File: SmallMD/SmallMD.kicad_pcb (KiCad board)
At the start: 2 copper layers, 178 parts, among them J1 Conn_01x02_Male, J2 Conn_01x02_Female, J3 Conn_01x10_Male, J4 Conn_01x02_Female, J5 Conn_01x04_Male, J6 Conn_01x04_Male, J7 Conn_01x10_Male, Q1 SSM6J808R, Q10 S8050, Q11 S8050, Q14 BSS138, Q15 BSS138, Q16 S8050, Q18 μPA2753GR, Q19 μPA2753GR, Q2 BSS138, Q3 SSM6J808R, Q4 SSM3J332R, Q5 SSM3J332R, Q6 S8050, Q7 S8050, Q8 SSM3J332R, Q9 SSM3J332R, SW1 SW_DIP_x05, SW2 SW_SPDT, SW3 SW_SPDT_White, SW4 SW_SPST, U1 AZ1084CD-3.3, U10 IR2302, U11 IR2302, U12 MAX3485, U2 AZ1084CD-5.0, U3 STM32C031K4T6, U4 MAX3485, U5 MAX3485, U6 LT6106, U7 MAX3485, U8 TLP2361, U9 TLP2361, Y1 48MHz

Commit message: 進捗
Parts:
- removed C15, C16: 470uF, Capacitor_SMD:C_Elec_8x10.2
- removed C8: ADJ_ST, Capacitor_SMD:C_0603_1608Metric
- removed D11, D12: Green, LED_SMD:LED_0603_1608Metric_Pad1.05x0.95mm_HandSolder
- removed D9: D_Zener, Diode_SMD:D_SOD-323_HandSoldering
- removed H1, H3: MountingHole_Pad, TestPoint:TestPoint_Pad_1.5x1.5mm
- removed H4, H6, H8: MountingHole, MountingHole:MountingHole_3.2mm_M3
- removed Q10, Q11, Q6, Q7: S8050, Package_TO_SOT_SMD:SOT-23
- removed Q4, Q5, Q8, Q9: SSM3J332R, Package_TO_SOT_SMD:SOT-23W
- removed R20, R21, R24, R25, R26, R27, R28, R29, R30: 10k, Resistor_SMD:R_0402_1005Metric
- removed R22, R32, R33: 1k, Resistor_SMD:R_0402_1005Metric
- removed R23: 100k, Resistor_SMD:R_0402_1005Metric
- added J8: Conn_01x06_Male, Connector_JST:JST_PH_B6B-PH-K_1x06_P2.00mm_Vertical, B.Cu at (87.4, 36.3)
- added JP5: SolderJumper_3_Bridged12, Jumper:SolderJumper-3_P2.0mm_Open_TrianglePad1.0x1.5mm_NumberLabels, F.Cu at (44.0, 47.0)
- added JP6: SolderJumper_3_Bridged12, Jumper:SolderJumper-3_P2.0mm_Open_TrianglePad1.0x1.5mm_NumberLabels, F.Cu at (44.0, 43.4)
- added R39: 40mR, Resistor_SMD:R_2512_6332Metric, F.Cu at (74.0, 11.0)
- added R46: 40mR, Resistor_SMD:R_2512_6332Metric, F.Cu at (74.0, 15.0)
- added R52: 40mR, Resistor_SMD:R_2512_6332Metric, F.Cu at (74.0, 19.0)
- added R53: 40mR, Resistor_SMD:R_2512_6332Metric, F.Cu at (74.0, 23.0)
- C17, C18: value 4.7uF -> 10uF; footprint Capacitor_SMD:C_0805_2012Metric_Pad1.18x1.45mm_HandSolder -> Capacitor_SMD:C_0805_2012Metric
- C2: value 0.1uF -> 10uF; footprint Capacitor_SMD:C_0402_1005Metric -> Capacitor_SMD:C_0805_2012Metric
- C7: value 1uF -> 10uF; footprint Capacitor_SMD:C_0402_1005Metric -> Capacitor_SMD:C_0805_2012Metric
- D1, D14, D7, D8: value SBR1A40SA -> 1N5819WS; footprint Diode_SMD:D_SMA_Handsoldering -> Diode_SMD:D_SOD-323_HandSoldering
- D15, D16: value SBR1A40SA -> SS2040FL; footprint Diode_SMD:D_SMA_Handsoldering -> Diode_SMD:D_SOD-123
- J1: footprint Connector_AMASS:AMASS_XT30PW-M_1x02_P2.50mm_Horizontal -> Connector_AMASS:AMASS_XT30U-M_1x02_P5.0mm_Vertical; moved to B.Cu
- J2, J4: footprint Connector_AMASS:AMASS_XT30PW-F_1x02_P2.50mm_Horizontal -> Connector_AMASS:AMASS_XT30U-F_1x02_P5.0mm_Vertical; moved to B.Cu
- J5, J6: footprint Connector_Molex:Molex_SPOX_5268-04A_1x04_P2.50mm_Horizontal -> Connector_Molex:Molex_SPOX_5267-04A_1x04_P2.50mm_Vertical; moved to B.Cu
- J7: footprint Connector_IDC:IDC-Header_2x05_P2.54mm_Horizontal -> Connector_IDC:IDC-Header_2x05_P2.54mm_Vertical; moved to B.Cu
- Y1: footprint Crystal:Crystal_SMD_HC49-SD_HandSoldering -> Crystal:Crystal_SMD_HC49-SD
- moved H5 132.9 mm to (5.00, 13.0)
- moved H9 122.3 mm to (55.0, 13.0)
- moved H7 119.5 mm to (5.00, 43.0)
- moved U1 109.5 mm to (40.2, 24.8), turned to 180 degrees
- moved Q3 106.1 mm to (80.1, 18.4), turned to 90 degrees
- moved U7 103.0 mm to (26.5, 20.8)
- moved SW2 100.0 mm to (14.0, 24.6)
- moved U12 97.6 mm to (56.0, 44.0)
- moved U2 97.6 mm to (52.8, 25.0), turned to 180 degrees
- moved U3 94.3 mm to (21.0, 32.7)
- moved Q1 91.9 mm to (80.1, 14.4)
- moved SW1 90.9 mm to (2.00, 26.0)
- moved C13 81.9 mm to (36.0, 36.0)
- moved U4 80.9 mm to (56.0, 32.0)
- moved C7 74.2 mm to (28.9, 106.0)
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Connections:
- net /12VBAT renamed /7.4VBAT
- net Encoder_invA renamed Maxon_RS422_invA
- net Encoder_invB renamed Maxon_RS422_invB
- net Encoder_invI renamed Maxon_RS422_invI
- C2 pad 1: /3.3VBUS -> +5V
- C5 pad 1: /3.3VSYS -> +3.3V
- C7 pad 1: /3.3VSYS -> +3.3V
- C7 pad 2: Net-(Q5-Pad1) -> GND
- D7 pad 2: /3.3VSYS -> +3.3V
- J3 pad 1: /3.3VBUS -> unconnected-(J3-Pad1)
- J7 pad 10: Encoder_I -> Maxon_RS422_I
- J7 pad 6: Encoder_A -> Maxon_RS422_A
- J7 pad 8: Encoder_B -> Maxon_RS422_B
- JP1 pad 1: Encoder_A -> Maxon_RS422_A
- JP2 pad 1: Encoder_B -> Maxon_RS422_B
- JP4 pad 1: Encoder_I -> Maxon_RS422_I
- R18 pad 2: /3.3VSYS -> +3.3V
- R35 pad 2: Encoder_A -> Maxon_RS422_A
- R37 pad 2: Encoder_B -> Maxon_RS422_B
- R73 pad 2: Encoder_I -> Maxon_RS422_I
- U1 pad 2: /3.3VSYS -> +3.3V
- U12 pad 1: Encoder_I -> Maxon_I
- U12 pad 6: Encoder_I -> Maxon_RS422_I
- U4 pad 1: Encoder_A -> Maxon_A
- U4 pad 6: Encoder_A -> Maxon_RS422_A
- U5 pad 1: Encoder_B -> Maxon_B
- U5 pad 6: Encoder_B -> Maxon_RS422_B

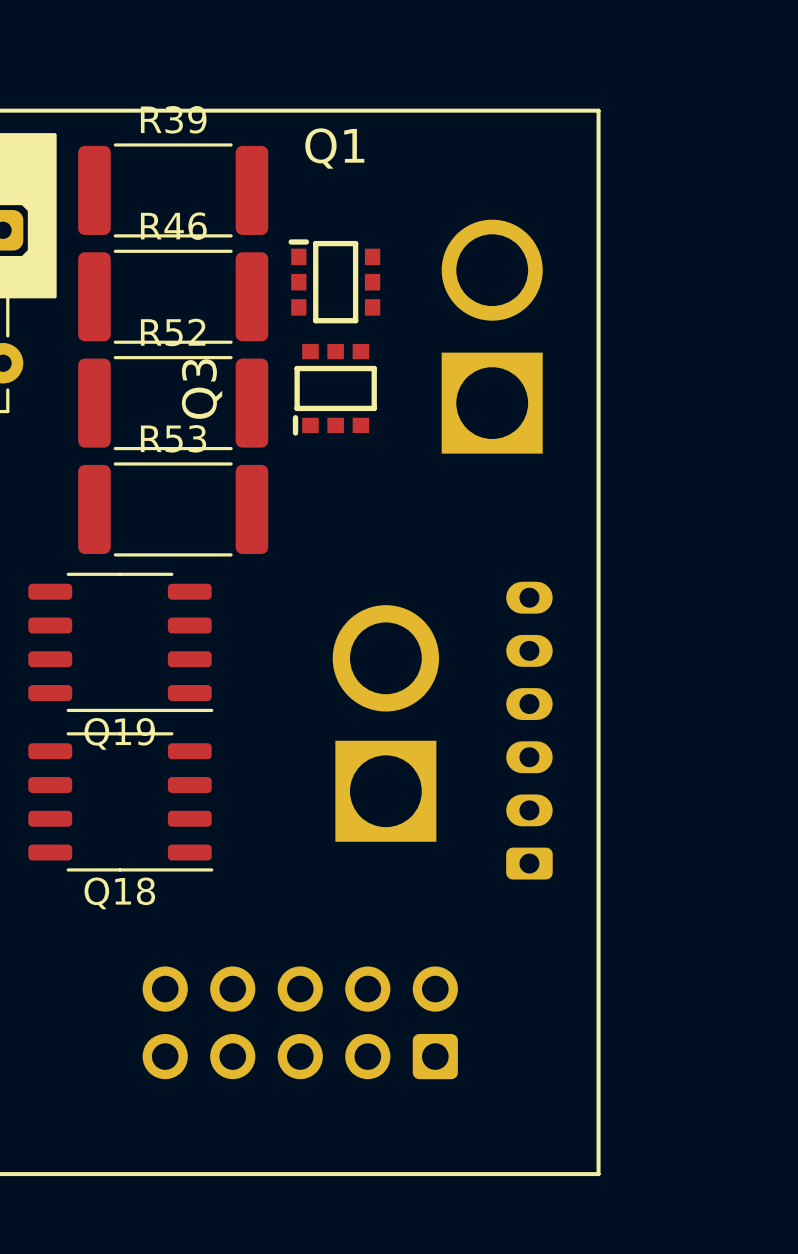
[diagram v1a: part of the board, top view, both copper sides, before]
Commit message: エンコーダー基板配線完了
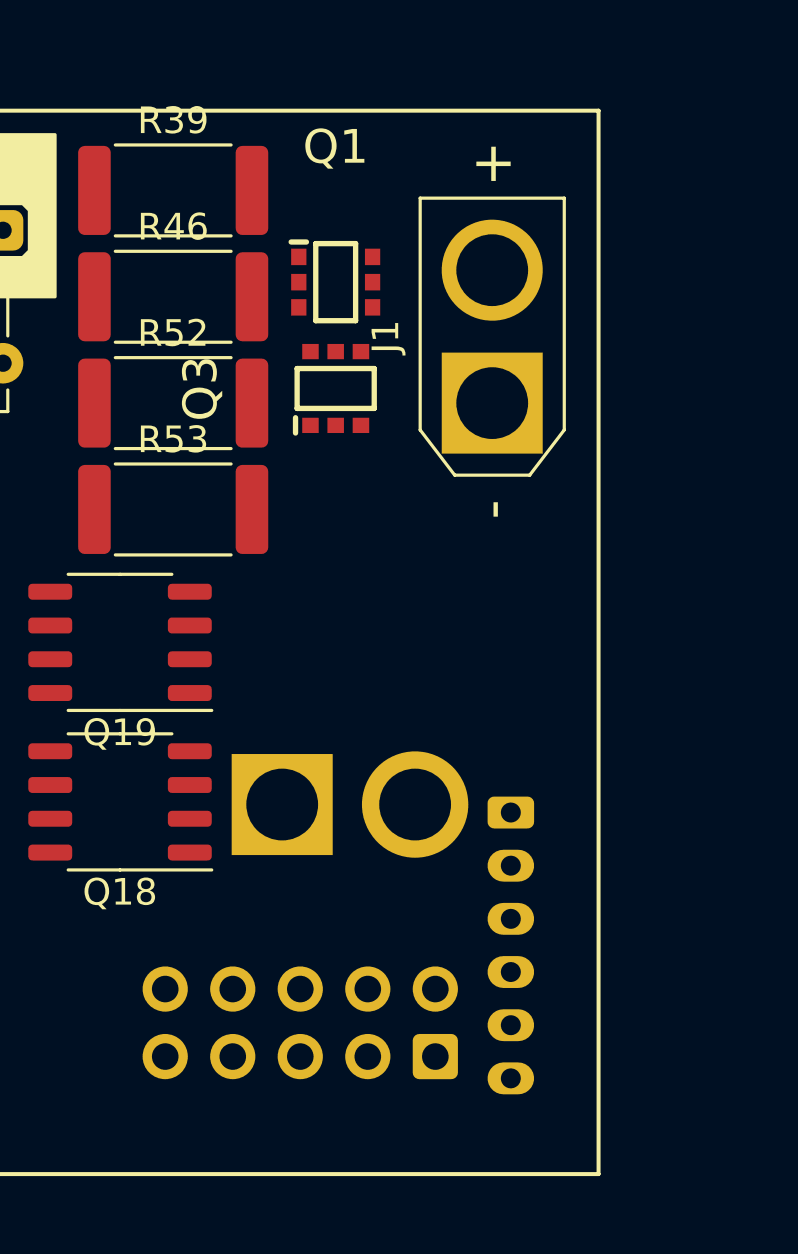
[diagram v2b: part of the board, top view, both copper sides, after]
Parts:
- J1: moved to F.Cu
- moved J4 3.93 mm to (78.1, 34.1), turned to 0 degrees
- moved J8 2.04 mm to (86.7, 34.4), turned to -90 degrees

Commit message: LargeMD
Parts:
- removed C10, C9: 22pF, Capacitor_SMD:C_0603_1608Metric
- removed R52, R53: 40mR, Resistor_SMD:R_2512_6332Metric
- added C8: 0.1uF, Capacitor_SMD:C_0402_1005Metric, F.Cu at (32.8, 63.6)
- added U13: NJU6319AE, Package_SO:SOP-8_3.9x4.9mm_P1.27mm, F.Cu at (27.1, 65.8)
- R39, R46: value 40mR -> 20mR
- Y1: value 48MHz -> 16MHz; footprint Crystal:Crystal_SMD_HC49-SD -> Crystal:Crystal_SMD_3225-4Pin_3.2x2.5mm_HandSoldering
- moved Y1 23.0 mm to (20.7, 65.9), turned to -90 degrees
- moved U3 3.22 mm to (18.1, 34.1)
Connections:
- U3 pad 2: unconnected-(U3-Pad2) -> OSC_IN
- U3 pad 6: unconnected-(U3-Pad6) -> NRST
- Y1 pad 1: OSC_OUT -> Net-(U13-Pad2)
- Y1 pad 2: OSC_IN -> GND

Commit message: 人力曲面配線中
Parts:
- removed J2: Conn_01x02_Female, Connector_AMASS:AMASS_XT30U-F_1x02_P5.0mm_Vertical
- C1, C11, C12, C17, C18, C19, C2, C20, C21, C22, C23, C24, C25, C26, C27, C28, C29, C3, C30, C4, C5, C6, C7, C8, D1, D14, D15, D16, D19, D20, D21, D22, D7, D8, Q14, Q15, Q16, Q2, R1, R10, R11, R12, R13, R14, R15, R16, R17, R18, R19, R2, R3, R31, R34, R35, R36, R37, R38, R4, R40, R41, R42, R43, R44, R45, R47, R48, R49, R5, R50, R51, R54, R56, R57, R58, R59, R6, R60, R63, R64, R65, R66, R68, R69, R7, R70, R71, R72, R73, R74, R75, R8, R9, U1, U10, U11, U12, U13, U2, U3, U4, U5, U6, U7, U8, U9, Y1: moved to B.Cu
- JP1, JP2, JP4: footprint Connector_PinHeader_2.54mm:PinHeader_1x02_P2.54mm_Vertical -> Jumper:SolderJumper-2_P1.3mm_Open_TrianglePad1.0x1.5mm; moved to B.Cu
- moved TP1 243.8 mm to (129.1, -84.7)
- moved TP5 243.8 mm to (136.3, -89.1)
- moved TP2 233.4 mm to (143.2, -87.4)
- moved H2 230.2 mm to (142.0, -76.7)
- moved TP4 228.3 mm to (146.5, -91.9)
- moved TP3 224.9 mm to (121.4, -86.9)
- moved D21 191.0 mm to (85.4, -22.0), turned to 180 degrees
- moved D14 187.0 mm to (58.9, -44.4), turned to 90 degrees
- moved R56 184.0 mm to (30.8, -36.0), turned to -90 degrees
- moved D22 183.9 mm to (85.4, -19.6)
- moved D20 182.5 mm to (76.4, -19.4)
- moved D5 181.4 mm to (30.9, -32.1)
- moved R57 179.9 mm to (30.8, -34.1), turned to -90 degrees
- moved D4 179.3 mm to (30.9, -33.9)
- moved D10 179.1 mm to (53.5, -29.5)
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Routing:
- net +5V: track 0.00 -> 103.7 mm
- net +3.3V: track 0.00 -> 99.4 mm, vias 0 -> 3
- net VCC: track 0.00 -> 65.6 mm, vias 0 -> 9
- net Akitsuki_A: track 0.00 -> 60.8 mm
- net Motor_A: track 0.00 -> 51.7 mm, vias 0 -> 51
- net Maxon_RS422_A: track 0.00 -> 47.4 mm
- net VDD: track 0.00 -> 45.3 mm, vias 0 -> 2
- net Maxon_RS422_invA: track 0.00 -> 44.9 mm
- net Akitsuki_B: track 0.00 -> 43.4 mm
- net Motor_B: track 0.00 -> 33.4 mm, vias 0 -> 59
- net Maxon_RS422_B: track 0.00 -> 32.1 mm
- net Maxon_RS422_invB: track 0.00 -> 29.1 mm
- net /S-S: track 0.00 -> 28.0 mm, vias 0 -> 1
- net Vdrive: track 0.00 -> 27.3 mm, vias 0 -> 21
- net Net-(Q19-Pad2): track 0.00 -> 25.1 mm, vias 0 -> 3
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- added copper zone on F.Cu, net /7.4VBAT
- added copper zone on F.Cu, net /S-S
- added copper zone on B.Cu, net GND
- added copper zone on F.Cu, net GND
- added copper zone on B.Cu, net Motor_A
- added copper zone on F.Cu, net Motor_A
- added copper zone on B.Cu, net Motor_B
- added copper zone on F.Cu, net Motor_B
- added copper zone on F.Cu, net VDD
- added copper zone on F.Cu, net Vdrive
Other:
- board outline added: 90 x 40 mm

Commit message: LargeMDほぼ完成
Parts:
- U3: value STM32C031K4T6 -> STM32G030K6T6
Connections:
- J3 pad 8: MainRX_STLinkTX -> MainRX1_STLinkTX
- J3 pad 9: MainTX_STLinkRX -> MainTX1_STLinkRX
- R49 pad 2: MainTX_RS485RX -> MainTX2_RS485RX
- U13 pad 6: Net-(U13-Pad6) -> unconnected-(U13-Pad6)
- U13 pad 7: Net-(U13-Pad6) -> unconnected-(U13-Pad7)
- U3 pad 13: unconnected-(U3-Pad13) -> PWM_A
- U3 pad 14: unconnected-(U3-Pad14) -> Encoder_A
- U3 pad 19: unconnected-(U3-Pad19) -> MainTX1_STLinkRX
- U3 pad 20: unconnected-(U3-Pad20) -> Encoder_B
- U3 pad 21: unconnected-(U3-Pad21) -> MainRX1_STLinkTX
- U3 pad 24: unconnected-(U3-Pad24) -> TMS
- U3 pad 25: unconnected-(U3-Pad25) -> TCK
- U3 pad 26: unconnected-(U3-Pad26) -> MainRX2_RS485TX
- U3 pad 9: unconnected-(U3-Pad9) -> MainTX2_RS485RX
- U7 pad 1: MainRX_RS485TX -> MainRX2_RS485TX
- U7 pad 4: MainTX_RS485RX -> MainTX2_RS485RX
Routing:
- net MainTX_RS485RX: track 4.57 -> 0.00 mm
- net MainTX2_RS485RX: track 0.00 -> 4.57 mm

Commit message: SmallMDほぼ完成
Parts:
- removed H5, H7, H9: MountingHole, MountingHole:MountingHole_3.2mm_M3
- removed TP1, TP2, TP3, TP4: TestPoint, TestPoint:TestPoint_THTPad_D2.0mm_Drill1.0mm
- moved C8 184.0 mm to (108.7, 82.1), turned to -90 degrees
- moved U13 178.9 mm to (105.4, 84.3), turned to 90 degrees
- moved Y1 177.9 mm to (105.2, 90.7), turned to 180 degrees
- moved TP5 157.4 mm to (114.6, 66.7)
- moved H2 150.6 mm to (93.4, 65.9)
- moved D14 133.3 mm to (131.7, 67.2)
- moved R69 127.1 mm to (138.6, 81.5), turned to 180 degrees
- moved R4 126.7 mm to (94.3, 68.6)
- moved R18 126.3 mm to (118.2, 71.1)
- moved C13 126.1 mm to (141.8, 74.7)
- moved C6 126.1 mm to (142.1, 72.2)
- moved D3 126.1 mm to (111.9, 60.9), turned to 180 degrees
- moved D5 126.1 mm to (111.9, 64.6), turned to 180 degrees
- moved D7 126.1 mm to (128.6, 74.8)
- moved JP2 126.1 mm to (135.0, 92.0)
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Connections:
- U3 pad 1: unconnected-(U3-Pad1) -> DIP_SW4
- U3 pad 11: unconnected-(U3-Pad11) -> MonitorLED0
- U3 pad 12: unconnected-(U3-Pad12) -> LED0
- U3 pad 15: unconnected-(U3-Pad15) -> LED1
- U3 pad 16: unconnected-(U3-Pad16) -> LED2
- U3 pad 22: unconnected-(U3-Pad22) -> V_Measure
- U3 pad 23: unconnected-(U3-Pad23) -> Current_Sence
- U3 pad 27: unconnected-(U3-Pad27) -> Maxon_I
- U3 pad 28: unconnected-(U3-Pad28) -> SHDN
- U3 pad 29: unconnected-(U3-Pad29) -> DIP_SW1
- U3 pad 30: unconnected-(U3-Pad30) -> PWM_B
- U3 pad 31: unconnected-(U3-Pad31) -> DIP_SW2
- U3 pad 32: unconnected-(U3-Pad32) -> DIP_SW3
- U3 pad 7: unconnected-(U3-Pad7) -> Slide_SW0
- U3 pad 8: unconnected-(U3-Pad8) -> DIP_SW0
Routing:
- net GND: track 16.0 -> 326.7 mm, vias 21 -> 344
- net +3.3V: track 99.4 -> 214.7 mm, vias 3 -> 9
- net Current_Sence: track 1.79 -> 50.2 mm, vias 0 -> 3
- net Maxon_I: track 0.00 -> 41.9 mm, vias 0 -> 2
- net NRST: track 0.00 -> 40.6 mm, vias 0 -> 1
- net SHDN: track 0.00 -> 38.9 mm, vias 0 -> 4
- net Encoder_B: track 0.00 -> 31.4 mm, vias 0 -> 1
- net Encoder_A: track 0.00 -> 26.9 mm, vias 0 -> 1
- net DIP_SW4: track 0.00 -> 22.2 mm, vias 0 -> 2
- net VCC: track 65.6 -> 87.5 mm, vias 9 -> 11
- net DIP_SW3: track 0.00 -> 21.8 mm, vias 0 -> 2
- net DIP_SW2: track 0.00 -> 20.5 mm, vias 0 -> 2
- net Net-(D5-Pad2): track 0.00 -> 20.3 mm, vias 0 -> 1
- net DIP_SW1: track 0.00 -> 20.0 mm, vias 0 -> 2
- net PWM_A: track 0.00 -> 19.0 mm, vias 0 -> 2
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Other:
- outline, holes or cut-outs redrawn
- board text added: "Designed by @cat_nekonekone"
- board text added: "Tomoshibi"
- board text added: "燈"

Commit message: 製造ファイル出力
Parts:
- moved TP5 0.75 mm to (115.3, 66.6)
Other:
- board text added: "3.3V"
- board text added: "5V"
- board text added: "ADC"
- board text added: "GND"
- board text added: "JLCJLCJLCJLC"
- board text added: "Motor"
- board text added: "NRST"
- board text added: "PA0"
- board text added: "PA1"
- board text added: "PA4"
- board text added: "PA5"
- board text added: "PB0"
- board text added: "PB1"
- board text added: "PB5"
- board text added: "PB7"
- board text added: "PB8"
- board text added: "PB9"
- board text added: "POWER"
- board text added: "RX1:PA10"
- board text added: "RX2:PA15"
- board text added: "TX1:PA9"
- board text added: "TX2:PA2"
- board text added: "[I_meas.]PA12"
- board text added: "[PWM_A]PA6"
- board text added: "[PWM_B]PB6"
- board text added: "[RS485]"
- board text added: "[SHDN]PB4"
- board text added: "[STLink]"
- board text added: "[V_meas.]PA11"
- board text added: "⇔"
